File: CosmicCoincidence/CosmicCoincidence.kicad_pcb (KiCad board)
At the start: 2 copper layers, 13 parts, among them J1 SJ-43515RS-SMT-TR, J2 SJ-43515RS-SMT-TR, J3 SJ-43515RS-SMT-TR, J4 SJ-43515RS-SMT-TR, J5 SJ-43515RS-SMT-TR, J6 SJ-43515RS-SMT-TR, J7 SJ-43515RS-SMT-TR, J8 SJ-43515RS-SMT-TR, J9 USB_C_Receptacle_USB2.0_14P, U1 SN74LVCC3245ADBR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

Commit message: Prototype 2
Addition of Power Control, Microsd card, and OLED I2C Screen
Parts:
- added J10: Micro_SD_Card, Connector_Card:microSD_HC_Molex_47219-2001, F.Cu at (176.4, 62.6)
- added J11: OLED Header, Connector_PinHeader_2.54mm:PinHeader_1x04_P2.54mm_Vertical, F.Cu at (182.0, 43.7)
- added MOSFET1: BSP315PH6327XTSA1, BSP315PH6327XTSA1:PG-SOT223-4_INF, B.Cu at (145.5, 35.5)
- added Q1: MMBT3904, Package_TO_SOT_SMD:SOT-23, B.Cu at (149.9, 42.0)
- added R10: 10k, Resistor_SMD:R_0805_2012Metric, B.Cu at (178.6, 79.0)
- added R11: 10k, Resistor_SMD:R_0805_2012Metric, B.Cu at (135.6, 83.5)
- added R3: 10k, Resistor_SMD:R_0805_2012Metric, B.Cu at (112.0, 79.0)
- added R4: 10k, Resistor_SMD:R_0805_2012Metric, B.Cu at (112.4, 92.5)
- added R5: 10k, Resistor_SMD:R_0805_2012Metric, B.Cu at (115.0, 114.9)
- added R6: 10k, Resistor_SMD:R_0805_2012Metric, B.Cu at (135.6, 114.9)
- added R7: 10k, Resistor_SMD:R_0805_2012Metric, B.Cu at (155.0, 114.9)
- added R8: 10k, Resistor_SMD:R_0805_2012Metric, B.Cu at (176.1, 114.9)
- added R9: 10k, Resistor_SMD:R_0805_2012Metric, B.Cu at (178.6, 92.0)
- R1: value 5.1kR -> 10K; moved to B.Cu
- R2: value 5.1kR -> 1K; moved to B.Cu
- moved R2 11.7 mm to (146.0, 41.5), turned to 0 degrees
- moved R1 9.22 mm to (151.0, 39.0), turned to 180 degrees
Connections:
- J1 pad 2: +5V -> +5VSwitched
- J2 pad 2: +5V -> +5VSwitched
- J3 pad 2: +5V -> +5VSwitched
- J4 pad 2: +5V -> +5VSwitched
- J5 pad 2: +5V -> +5VSwitched
- J6 pad 2: +5V -> +5VSwitched
- J7 pad 2: +5V -> +5VSwitched
- J8 pad 2: +5V -> +5VSwitched
- R1 pad 1: Net-(J9-CC1) -> Net-(MOSFET1-G)
- R1 pad 2: GND -> +5V
- R2 pad 1: Net-(J9-CC2) -> Net-(U2-GPIO22)
- R2 pad 2: GND -> Net-(Q1-C)
- U1 pad 1: +5V -> +5VSwitched
- U2 pad 18: unconnected-(U2-GND-Pad18) -> GND
- U2 pad 21: unconnected-(U2-GPIO16-Pad21) -> Net-(J10-DO)
- U2 pad 22: unconnected-(U2-GPIO17-Pad22) -> Net-(J10-CS)
- U2 pad 23: unconnected-(U2-GND-Pad23) -> GND
- U2 pad 24: unconnected-(U2-GPIO18-Pad24) -> Net-(J10-SCLK)
- U2 pad 25: unconnected-(U2-GPIO19-Pad25) -> Net-(J10-DI)
- U2 pad 26: unconnected-(U2-GPIO20-Pad26) -> Net-(J11-SDA)
- U2 pad 27: unconnected-(U2-GPIO21-Pad27) -> Net-(J11-SCL)
- U2 pad 28: unconnected-(U2-GND-Pad28) -> GND
- U2 pad 29: unconnected-(U2-GPIO22-Pad29) -> Net-(U2-GPIO22)
- U2 pad 31: unconnected-(U2-GPIO26_ADC0-Pad31) -> Net-(J9-CC2)
- U2 pad 32: unconnected-(U2-GPIO27_ADC1-Pad32) -> Net-(J9-CC1)
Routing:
- net +5VSwitched: track 0.00 -> 195.3 mm, vias 0 -> 6
- net +5V: track 215.2 -> 66.8 mm, vias 5 -> 1
- net GND: track 330.2 -> 452.2 mm, vias 6 -> 15
- net Net-(J10-DO): track 0.00 -> 39.8 mm
- net Net-(J11-SDA): track 0.00 -> 37.0 mm
- net Net-(J9-CC2): track 3.25 -> 39.7 mm
- net Net-(J11-SCL): track 0.00 -> 35.5 mm
- net +3V3: track 59.0 -> 92.6 mm, vias 2 -> 4
- net Net-(J10-CS): track 0.00 -> 31.2 mm
- net Net-(J9-CC1): track 4.02 -> 32.6 mm
- net Net-(J10-SCLK): track 0.00 -> 25.8 mm
- net Net-(U2-GPIO22): track 0.00 -> 25.6 mm, vias 0 -> 1
- net Net-(J10-DI): track 0.00 -> 23.8 mm, vias 0 -> 2
- net Net-(MOSFET1-G): track 0.00 -> 6.45 mm
- net Net-(J1-R1): track 41.2 -> 46.3 mm, vias 0 -> 1
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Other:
- board outline added: 75 x 100 mm

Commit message: Updated PCB Design (Still no switch footprint)
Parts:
- MOSFET1, Q1, R1, R10, R11, R2, R3, R4, R5, R6, R7, R8, R9: moved to F.Cu
- moved R10 25.9 mm to (159.8, 96.7), turned to 90 degrees
- moved MOSFET1 21.5 mm to (166.0, 42.0), turned to -90 degrees
- moved R2 21.3 mm to (163.0, 54.4), turned to 90 degrees
- moved R3 16.8 mm to (128.4, 82.8), turned to -90 degrees
- moved R4 16.1 mm to (128.5, 92.5), turned to 90 degrees
- moved Q1 15.2 mm to (163.5, 48.9), turned to 90 degrees
- moved R1 11.1 mm to (161.5, 35.5)
- moved R5 10.4 mm to (125.0, 112.0), turned to 90 degrees
- moved R6 9.30 mm to (142.7, 108.9), turned to 90 degrees
- moved R9 8.90 mm to (172.5, 98.5), turned to 0 degrees
- moved R8 8.85 mm to (167.9, 111.6)
- moved R7 8.71 mm to (148.7, 108.9)
- moved R11 6.02 mm to (136.1, 89.5)
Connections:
- net +5VSwitched renamed Net-(J1-T)
- Q1 pad 1: Net-(MOSFET1-G) -> +3V3
- Q1 pad 2: +3V3 -> Net-(Q1-E)
- Q1 pad 3: Net-(Q1-C) -> Net-(MOSFET1-G)
- R2 pad 2: Net-(Q1-C) -> Net-(Q1-E)
- U2 pad 13: unconnected-(U2-GND-Pad13) -> GND
- U2 pad A: (no net) -> GND
- U2 pad B: (no net) -> GND
- U2 pad C: (no net) -> GND
- U2 pad D: (no net) -> GND
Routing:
- net GND: track 452.2 -> 26.5 mm, vias 15 -> 5
- net Net-(U2-GPIO22): track 25.6 -> 12.2 mm, vias 1 -> 0
- net +5V: track 66.8 -> 57.7 mm, vias 1 -> 2
- net Net-(MOSFET1-G): track 6.45 -> 13.0 mm
- net Net-(U1-DIR): track 15.7 -> 21.5 mm, vias 2 -> 3
- net +3V3: track 92.6 -> 98.0 mm, vias 4 -> 5
- net Net-(J1-R1): track 46.3 -> 41.4 mm, vias 1 -> 0
- net Net-(J7-R1): track 37.5 -> 33.1 mm, vias 1 -> 0
- net Net-(Q1-E): track 0.00 -> 4.23 mm
- net Net-(J8-R1): track 42.2 -> 38.1 mm, vias 1 -> 0
- net Net-(J6-R1): track 39.7 -> 36.2 mm, vias 1 -> 0
- net Net-(J1-T): track 195.3 -> 191.7 mm, vias 6 -> 5
- net Net-(J5-R1): track 23.0 -> 19.5 mm, vias 1 -> 0
- net Net-(Q1-C): track 2.29 -> 0.00 mm
- net Net-(J2-R1): track 49.7 -> 51.9 mm, vias 1 -> 0
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- added copper zone on F.Cu, net GND

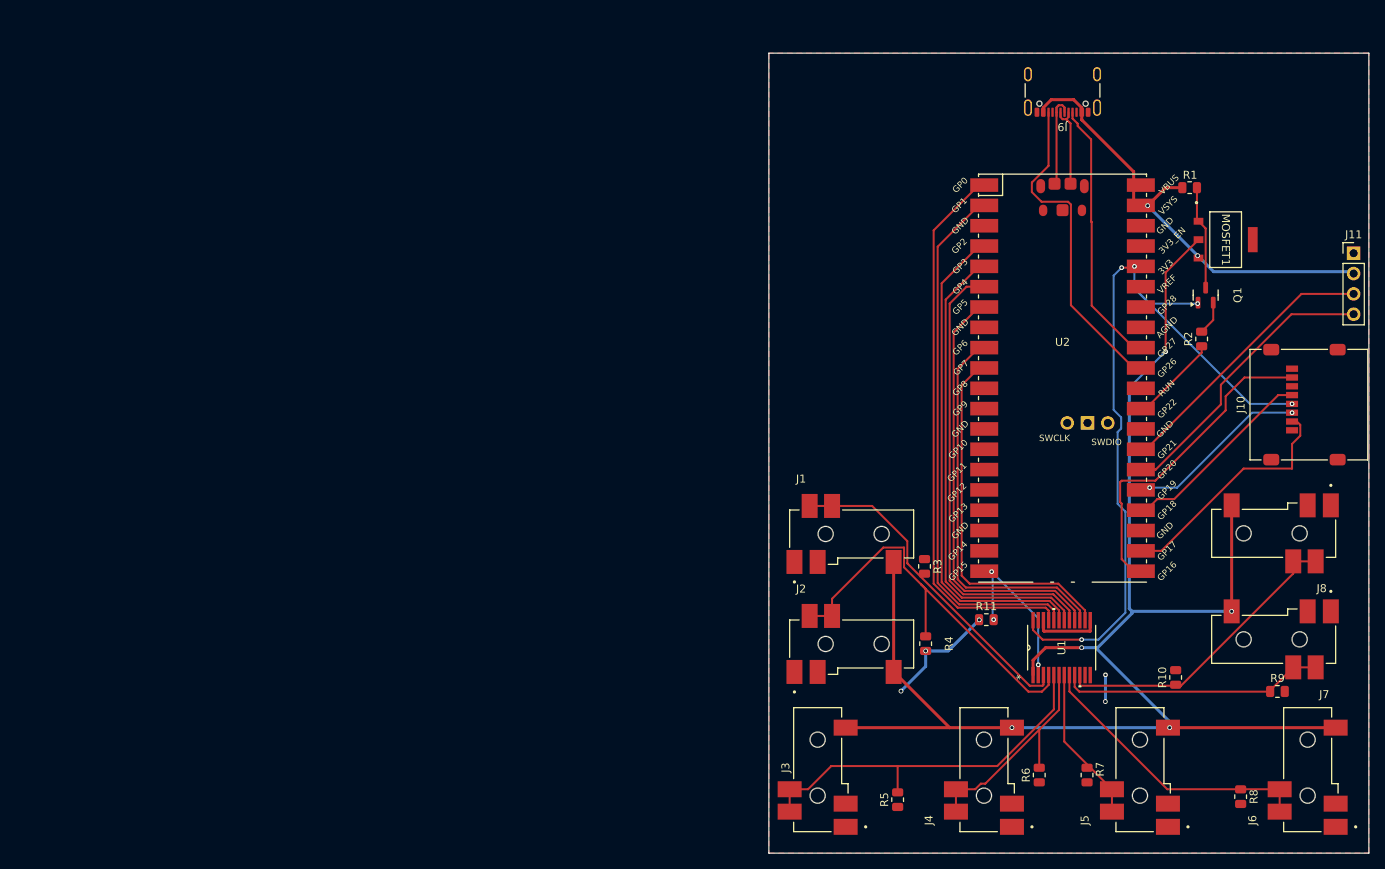
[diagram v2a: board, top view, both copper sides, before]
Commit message: clean up schematic; add spice test schematic; change power switching circuit
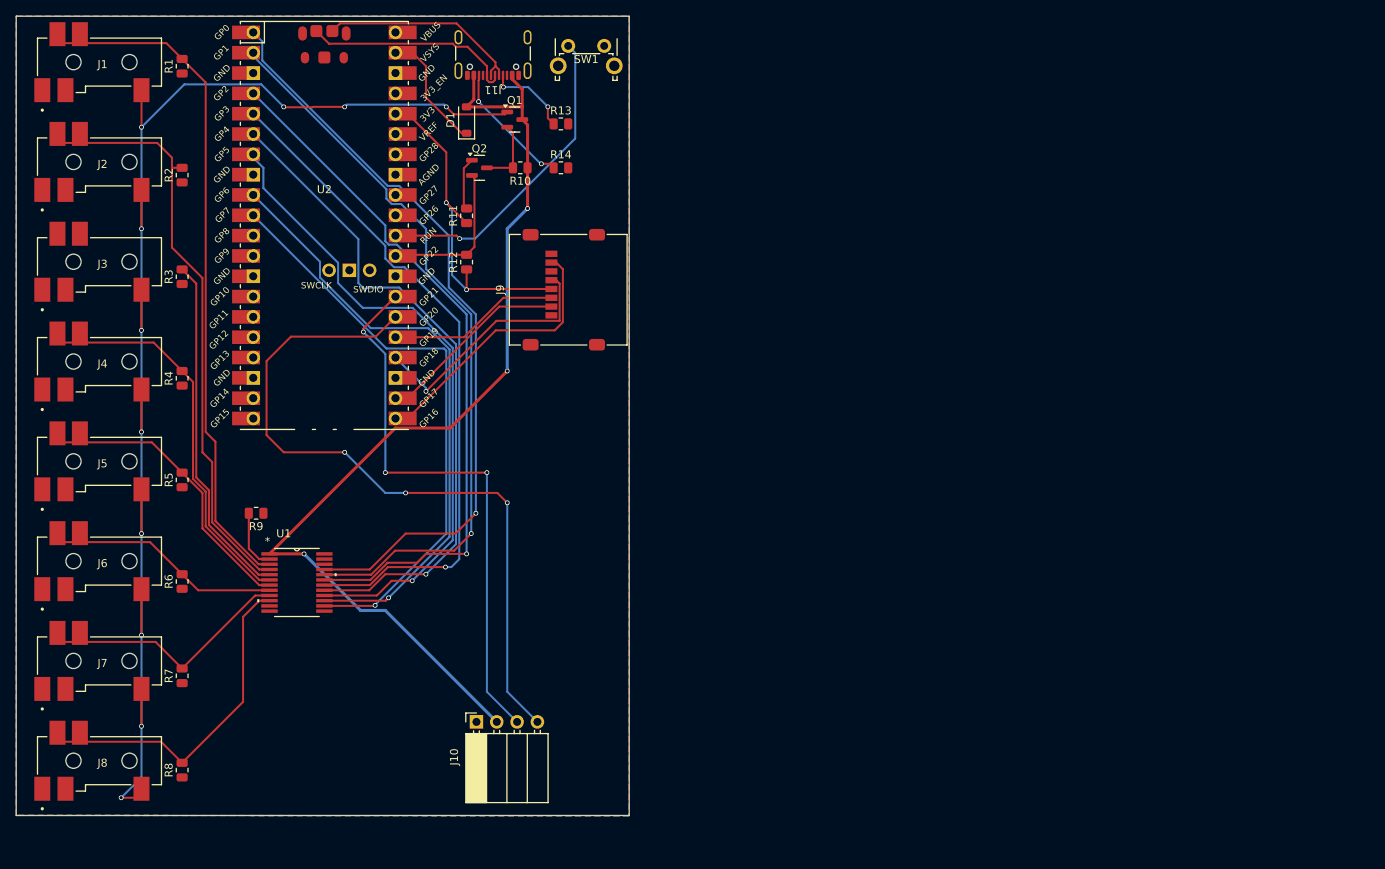
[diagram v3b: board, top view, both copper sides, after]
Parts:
- removed MOSFET1: BSP315PH6327XTSA1, BSP315PH6327XTSA1:PG-SOT223-4_INF
- added D1: D_Schottky, Diode_SMD:D_SOD-123, F.Cu at (71.1, 27.1)
- added Q2: MMBT3904, Package_TO_SOT_SMD:SOT-23, F.Cu at (72.7, 33.0)
- added R12: 22k, Resistor_SMD:R_0805_2012Metric, F.Cu at (71.1, 44.8)
- added R13: 5k1, Resistor_SMD:R_0805_2012Metric, F.Cu at (82.9, 27.5)
- added R14: 5k1, Resistor_SMD:R_0805_2012Metric, F.Cu at (82.9, 33.0)
- added SW1: Reset, Button_Switch_THT:SW_Tactile_SPST_Angled_PTS645Vx83-2LFS, F.Cu at (83.8, 17.8)
- J10: value Micro_SD_Card -> OLED Header; footprint Connector_Card:microSD_HC_Molex_47219-2001 -> Connector_PinSocket_2.54mm:PinSocket_1x04_P2.54mm_Horizontal
- J11: value OLED Header -> USB_C_Receptacle_USB2.0_14P; footprint Connector_PinHeader_2.54mm:PinHeader_1x04_P2.54mm_Vertical -> Connector_USB:USB_C_Receptacle_GCT_USB4105-xx-A_16P_TopMnt_Horizontal
- J9: value USB_C_Receptacle_USB2.0_14P -> Micro_SD_Card; footprint Connector_USB:USB_C_Receptacle_GCT_USB4105-xx-A_16P_TopMnt_Horizontal -> Connector_Card:microSD_HC_Molex_47219-2001
- Q1: value MMBT3904 -> PMOS
- R1: value 10K -> 10k
- R11: value 10k -> 22k
- R2: value 1K -> 10k
- moved J8 164.9 mm to (18.1, 110.6), turned to 0 degrees
- moved J6 164.4 mm to (18.1, 85.7), turned to 0 degrees
- moved J7 161.4 mm to (18.1, 98.2), turned to 0 degrees
- moved J5 146.9 mm to (18.1, 73.2), turned to 0 degrees
- moved J4 133.0 mm to (18.1, 60.7), turned to 0 degrees
- moved R8 132.4 mm to (35.6, 108.3), turned to 90 degrees
- moved R9 129.6 mm to (44.8, 76.2), turned to 180 degrees
- moved R2 129.1 mm to (35.6, 33.9)
- moved R1 126.9 mm to (35.6, 20.3), turned to 90 degrees
- moved J3 120.8 mm to (18.1, 48.3), turned to 0 degrees
- moved R7 113.8 mm to (35.6, 96.5), turned to 90 degrees
- moved J2 111.7 mm to (18.1, 35.8)
- moved J10 111.4 mm to (72.3, 102.3)
- moved J1 111.0 mm to (18.1, 23.3)
- moved J11 110.7 mm to (74.4, 17.8), turned to 180 degrees
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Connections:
- net Net-(U1-B1) renamed /GPIO0
- net Net-(U1-B2) renamed /GPIO1
- net Net-(U1-B3) renamed /GPIO2
- net Net-(U1-B4) renamed /GPIO3
- net Net-(U1-B5) renamed /GPIO4
- net Net-(U1-B6) renamed /GPIO5
- net Net-(U1-B7) renamed /GPIO6
- net Net-(U1-B8) renamed /GPIO7
- J1 pad 2: Net-(J1-T) -> +5V_SWITCHED
- J1 pad 3: Net-(J1-R1) -> /D0
- J1 pad 6: Net-(J1-R1) -> /D0
- J10 pad 1: unconnected-(J10-X-Pad1) -> GND
- J10 pad 2: Net-(J10-CS) -> +5V
- J10 pad 3: Net-(J10-DI) -> /SCL
- J10 pad 4: +3V3 -> /SDA
- J2 pad 2: Net-(J1-T) -> +5V_SWITCHED
- J2 pad 3: Net-(J2-R1) -> /D1
- J2 pad 6: Net-(J2-R1) -> /D1
- J3 pad 2: Net-(J1-T) -> +5V_SWITCHED
- J3 pad 3: Net-(J3-R1) -> /D2
- J3 pad 6: Net-(J3-R1) -> /D2
- J4 pad 2: Net-(J1-T) -> +5V_SWITCHED
- J4 pad 3: Net-(J4-R1) -> /D3
- J4 pad 6: Net-(J4-R1) -> /D3
- J5 pad 2: Net-(J1-T) -> +5V_SWITCHED
- J5 pad 3: Net-(J5-R1) -> /D4
- J5 pad 6: Net-(J5-R1) -> /D4
- J6 pad 2: Net-(J1-T) -> +5V_SWITCHED
- J6 pad 3: Net-(J6-R1) -> /D5
- J6 pad 6: Net-(J6-R1) -> /D5
- J7 pad 2: Net-(J1-T) -> +5V_SWITCHED
- J7 pad 3: Net-(J7-R1) -> /D6
- J7 pad 6: Net-(J7-R1) -> /D6
- J8 pad 2: Net-(J1-T) -> +5V_SWITCHED
- J8 pad 3: Net-(J8-R1) -> /D7
- J8 pad 6: Net-(J8-R1) -> /D7
- Q1 pad 1: +3V3 -> +5V_SWITCHED
- Q1 pad 2: Net-(Q1-E) -> Net-(Q1-G)
- Q1 pad 3: Net-(MOSFET1-G) -> +5V
- R1 pad 1: Net-(MOSFET1-G) -> GND
- R1 pad 2: +5V -> /D0
- R10 pad 1: Net-(J8-R1) -> +5V
- R10 pad 2: GND -> Net-(Q1-G)
- R11 pad 1: GND -> +3V3
- R11 pad 2: Net-(U1-DIR) -> Net-(Q2-B)
- R2 pad 1: Net-(U2-GPIO22) -> GND
- R2 pad 2: Net-(Q1-E) -> /D1
- R3 pad 2: Net-(J1-R1) -> /D2
- R4 pad 2: Net-(J2-R1) -> /D3
- R5 pad 2: Net-(J3-R1) -> /D4
- R6 pad 2: Net-(J4-R1) -> /D5
- R7 pad 1: Net-(J5-R1) -> GND
- R7 pad 2: GND -> /D6
- R8 pad 1: Net-(J6-R1) -> GND
- R8 pad 2: GND -> /D7
- R9 pad 1: Net-(J7-R1) -> GND
- R9 pad 2: GND -> /GPIO15
- U1 pad 1: Net-(J1-T) -> +5V
- U1 pad 10: Net-(J8-R1) -> /D7
- U1 pad 2: Net-(U1-DIR) -> /GPIO15
- U1 pad 3: Net-(J1-R1) -> /D0
- U1 pad 4: Net-(J2-R1) -> /D1
- U1 pad 5: Net-(J3-R1) -> /D2
- U1 pad 6: Net-(J4-R1) -> /D3
- U1 pad 7: Net-(J5-R1) -> /D4
- U1 pad 8: Net-(J6-R1) -> /D5
- U1 pad 9: Net-(J7-R1) -> /D6
- U2 pad 20: Net-(U1-DIR) -> unconnected-(U2-GPIO15-Pad20)
- U2 pad 21: Net-(J10-DO) -> /MISO
- U2 pad 22: Net-(J10-CS) -> /CS
- U2 pad 24: Net-(J10-SCLK) -> /SCLK
- U2 pad 25: Net-(J10-DI) -> /MOSI
- U2 pad 26: Net-(J11-SDA) -> /SDA
- U2 pad 27: Net-(J11-SCL) -> /SCL
- U2 pad 29: Net-(U2-GPIO22) -> /GPIO22
- U2 pad 31: Net-(J9-CC2) -> /ADC0
- U2 pad 32: Net-(J9-CC1) -> /ADC1
- U2 pad 33: unconnected-(U2-AGND-Pad33) -> GND
- U2 pad 38: unconnected-(U2-GND-Pad38) -> GND
- U2 pad 39: +5V -> Net-(D1-K)
- U2 pad 40: +5V -> unconnected-(U2-VBUS-Pad40)
- U2 pad 8: unconnected-(U2-GND-Pad8) -> GND
- U2 pad A: GND -> (no net)
- U2 pad B: GND -> (no net)
- U2 pad C: GND -> (no net)
- U2 pad D: GND -> (no net)
- U2 pad TP2: Net-(U2-USB_DM) -> /USB_DM
- U2 pad TP3: Net-(U2-USB_DP) -> /USB_DP
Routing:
- net Net-(J1-T): track 191.7 -> 0.00 mm, vias 5 -> 0
- net +5V_SWITCHED: track 0.00 -> 166.4 mm, vias 0 -> 11
- net /SDA: track 0.00 -> 90.2 mm, vias 0 -> 3
- net /D0: track 0.00 -> 84.9 mm
- net /D1: track 0.00 -> 73.6 mm
- net /SCL: track 0.00 -> 70.2 mm, vias 0 -> 3
- net +5V: track 57.7 -> 126.4 mm, vias 2 -> 3
- net +3V3: track 98.0 -> 43.3 mm, vias 5 -> 2
- net Net-(J2-R1): track 51.9 -> 0.00 mm
- net /D3: track 0.00 -> 48.4 mm
- net Net-(J3-R1): track 47.5 -> 0.00 mm
- net /D2: track 0.00 -> 44.0 mm
- net /D7: track 0.00 -> 42.2 mm
- net Net-(J1-R1): track 41.4 -> 0.00 mm
- net Net-(J9-CC2): track 40.0 -> 0.00 mm
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- added copper zone on B.Cu, net GND
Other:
- board size 75 x 100 mm -> 76.6 x 99.9 mm
